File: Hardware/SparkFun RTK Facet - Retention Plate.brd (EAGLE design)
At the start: 58 x 20 mm, 6 parts

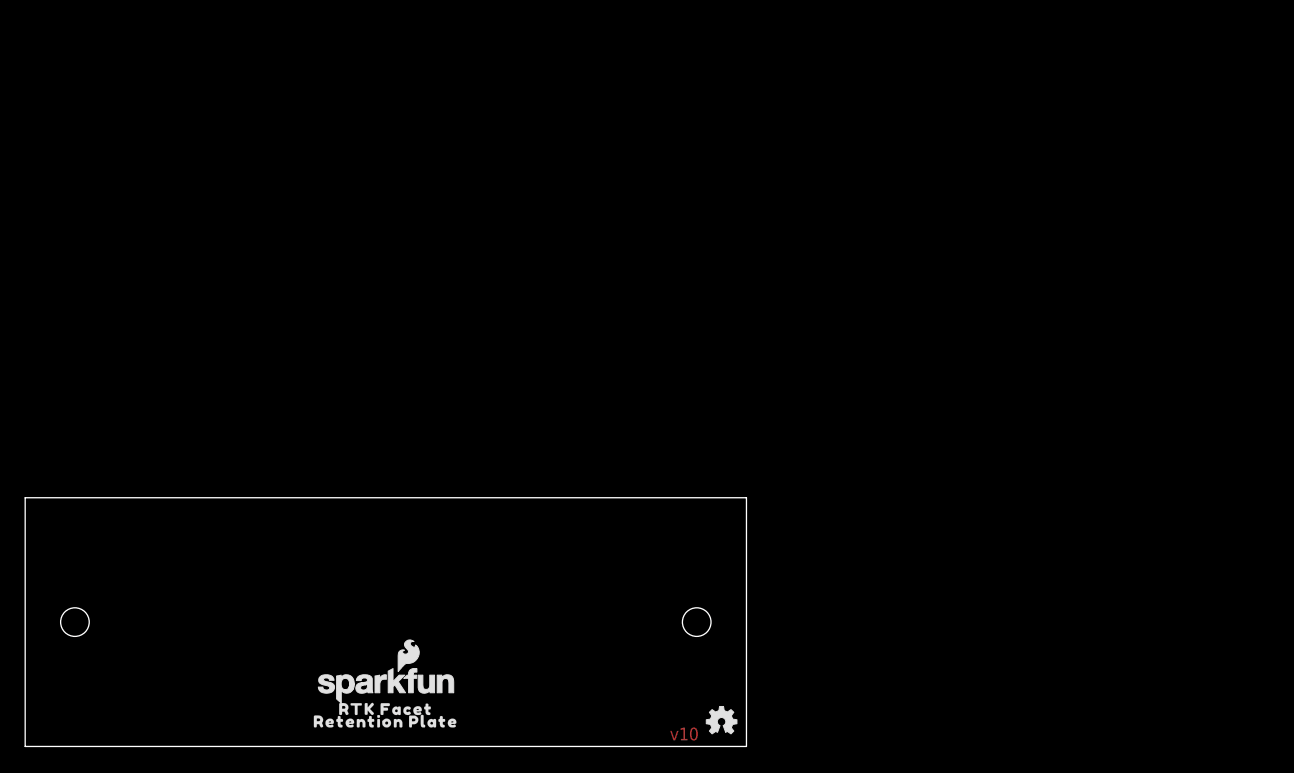
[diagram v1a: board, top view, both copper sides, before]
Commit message: Adding retention plate
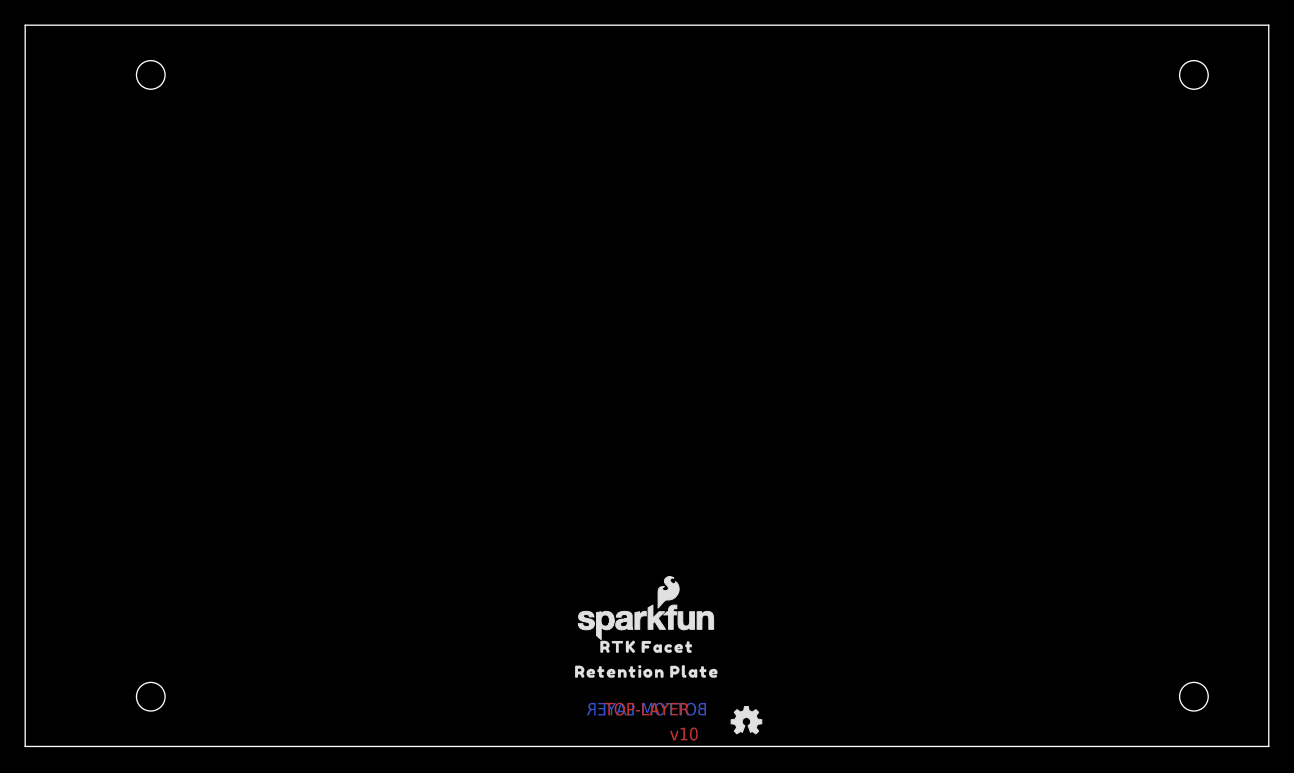
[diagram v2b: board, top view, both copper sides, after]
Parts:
- moved U$3 77.5 mm to (142.2, 50.8)
- moved U$2 21.6 mm to (50.0, 8.00)
- moved LOGO5 21.5 mm to (50.0, 10.0)
- moved U$1 21.4 mm to (50.0, 6.00)
- moved LOGO3 2.00 mm to (58.0, 2.00)
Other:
- board size 58 x 20 mm -> 100 x 58 mm
- board text added: "1.6mm PCB Thickness"
- board text added: "BOTTOM-LAYER"
- board text added: "TOP-LAYER"
- board text removed: "0.8mm PCB Thickness"
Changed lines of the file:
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@@
 <?xml version="1.0" encoding="utf-8"?>
 <!DOCTYPE eagle SYSTEM "eagle.dtd">
-<eagle version="9.5.2">
+<eagle version="9.6.2">
 <drawing>
 <settings>
@@
 <setting verticaltext="up"/>
 </settings>
-<grid distance="0.05" unitdist="inch" unit="inch" style="lines" multiple="1" display="yes" altdistance="0.005" altunitdist="inch" altunit="inch"/>
+<grid distance="1" unitdist="mm" unit="mm" style="lines" multiple="1" display="yes" altdistance="0.1" altunitdist="mm" altunit="mm"/>
 <layers>
 <layer number="1" name="Top" color="4" fill="1" visible="yes" active="yes"/>
@@
 <layer number="47" name="Measures" color="7" fill="1" visible="no" active="yes"/>
 <layer number="48" name="Document" color="7" fill="1" visible="no" active="yes"/>
-<layer number="49" name="Reference" color="7" fill="1" visible="no" active="yes"/>
+<layer number="49" name="Reference" color="7" fill="1" visible="yes" active="yes"/>
 <layer number="50" name="dxf" color="7" fill="1" visible="no" active="yes"/>
 <layer number="51" name="tDocu" color="6" fill="1" visible="yes" active="yes"/>
@@
 <plain>
 <text x="53" y="1" size="1.016" layer="1" font="vector" ratio="20" rot="R180" align="center">v10</text>
-<rectangle x1="0" y1="0" x2="2" y2="22" layer="39"/>
-<rectangle x1="0" y1="0" x2="2" y2="22" layer="40"/>
-<rectangle x1="48" y1="0" x2="50" y2="22" layer="40"/>
-<rectangle x1="48" y1="0" x2="50" y2="22" layer="39"/>
-<wire x1="29" y1="26" x2="29" y2="-5" width="0.05" layer="51"/>
-<wire x1="0" y1="0" x2="0" y2="20" width="0.05" layer="20"/>
-<wire x1="0" y1="20" x2="58" y2="20" width="0.05" layer="20"/>
-<wire x1="58" y1="20" x2="58" y2="0" width="0.05" layer="20"/>
-<wire x1="58" y1="0" x2="0" y2="0" width="0.05" layer="20"/>
-<hole x="54" y="10" drill="2.3"/>
-<hole x="4" y="10" drill="2.3"/>
-<text x="68.58" y="22.86" size="1.778" layer="51" font="vector" ratio="15">0.8mm PCB Thickness</text>
+<wire x1="50" y1="60" x2="50" y2="-2" width="0.05" layer="51"/>
+<wire x1="0" y1="0" x2="0" y2="58" width="0.05" layer="20"/>
+<wire x1="0" y1="58" x2="100" y2="58" width="0.05" layer="20"/>
+<wire x1="100" y1="58" x2="100" y2="0" width="0.05" layer="20"/>
+<wire x1="100" y1="0" x2="0" y2="0" width="0.05" layer="20"/>
+<hole x="93.98" y="4" drill="2.3"/>
+<hole x="10.1" y="4" drill="2.3"/>
+<text x="144.78" y="36.83" size="1.778" layer="51" font="vector" ratio="15">1.6mm PCB Thickness</text>
+<hole x="10.1" y="54" drill="2.3"/>
+<hole x="93.98" y="54" drill="2.3"/>
+<text x="50" y="3" size="1" layer="1" font="vector" ratio="20" align="center">TOP-LAYER</text>
+<text x="50" y="3" size="1" layer="16" font="vector" ratio="20" rot="MR0" align="center">BOTTOM-LAYER</text>
+<wire x1="-2" y1="29" x2="102" y2="29" width="0.05" layer="51"/>
+<dimension x1="10.1" y1="4" x2="0" y2="0" x3="5.05" y3="-2" textsize="0.5" textratio="15" layer="47" dtype="horizontal" width="0.05"/>
+<dimension x1="100" y1="0" x2="93.98" y2="4" x3="96.99" y3="-2" textsize="0.5" textratio="15" layer="47" dtype="horizontal" width="0.05"/>
+<dimension x1="100" y1="0" x2="93.98" y2="4" x3="103" y3="2" textsize="0.5" textratio="15" layer="47" dtype="vertical" width="0.05"/>
+<dimension x1="0" y1="0" x2="10.1" y2="4" x3="-3" y3="2" textsize="0.5" textratio="15" layer="47" dtype="vertical" width="0.05"/>
+<dimension x1="0" y1="58" x2="10.1" y2="54" x3="-2" y3="56" textsize="0.5" textratio="15" layer="47" dtype="vertical" width="0.05"/>
 </plain>
 <attributes>
@@
 <attribute name="REV" value="" x="-2.57" y="-29.5" size="1.778" layer="27" display="off"/>
 </element>
-<element name="LOGO3" library="SparkFun-Aesthetics" package="OSHW-LOGO-MINI" value="OSHW-LOGOMINI" x="56" y="2" smashed="yes"/>
-<element name="LOGO5" library="SparkFun-Aesthetics" package="SFE_LOGO_NAME_FLAME_.1" value="SFE_LOGO_NAME_FLAME.1_INCH" x="29.1" y="4.9" smashed="yes"/>
-<element name="U$1" library="output" package="RETENTION_PLATE1" value="" x="29" y="2" smashed="yes"/>
-<element name="U$2" library="output" package="RTK_FACET0" value="" x="29" y="3" smashed="yes"/>
-<element name="U$3" library="SparkFun-Aesthetics" package="ORDERING_INSTRUCTIONS" value="" x="66.04" y="36.83" smashed="yes"/>
+<element name="LOGO3" library="SparkFun-Aesthetics" package="OSHW-LOGO-MINI" value="OSHW-LOGOMINI" x="58" y="2" smashed="yes"/>
+<element name="LOGO5" library="SparkFun-Aesthetics" package="SFE_LOGO_NAME_FLAME_.1" value="SFE_LOGO_NAME_FLAME.1_INCH" x="50" y="10" smashed="yes"/>
+<element name="U$1" library="output" package="RETENTION_PLATE1" value="" x="50" y="6" smashed="yes"/>
+<element name="U$2" library="output" package="RTK_FACET0" value="" x="50" y="8" smashed="yes"/>
+<element name="U$3" library="SparkFun-Aesthetics" package="ORDERING_INSTRUCTIONS" value="" x="142.24" y="50.8" smashed="yes"/>
 </elements>
 <signals>
